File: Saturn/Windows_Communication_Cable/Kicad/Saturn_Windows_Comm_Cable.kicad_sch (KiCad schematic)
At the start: 8 parts, among them J1 SegaSaturn, J2 Windows_RS232

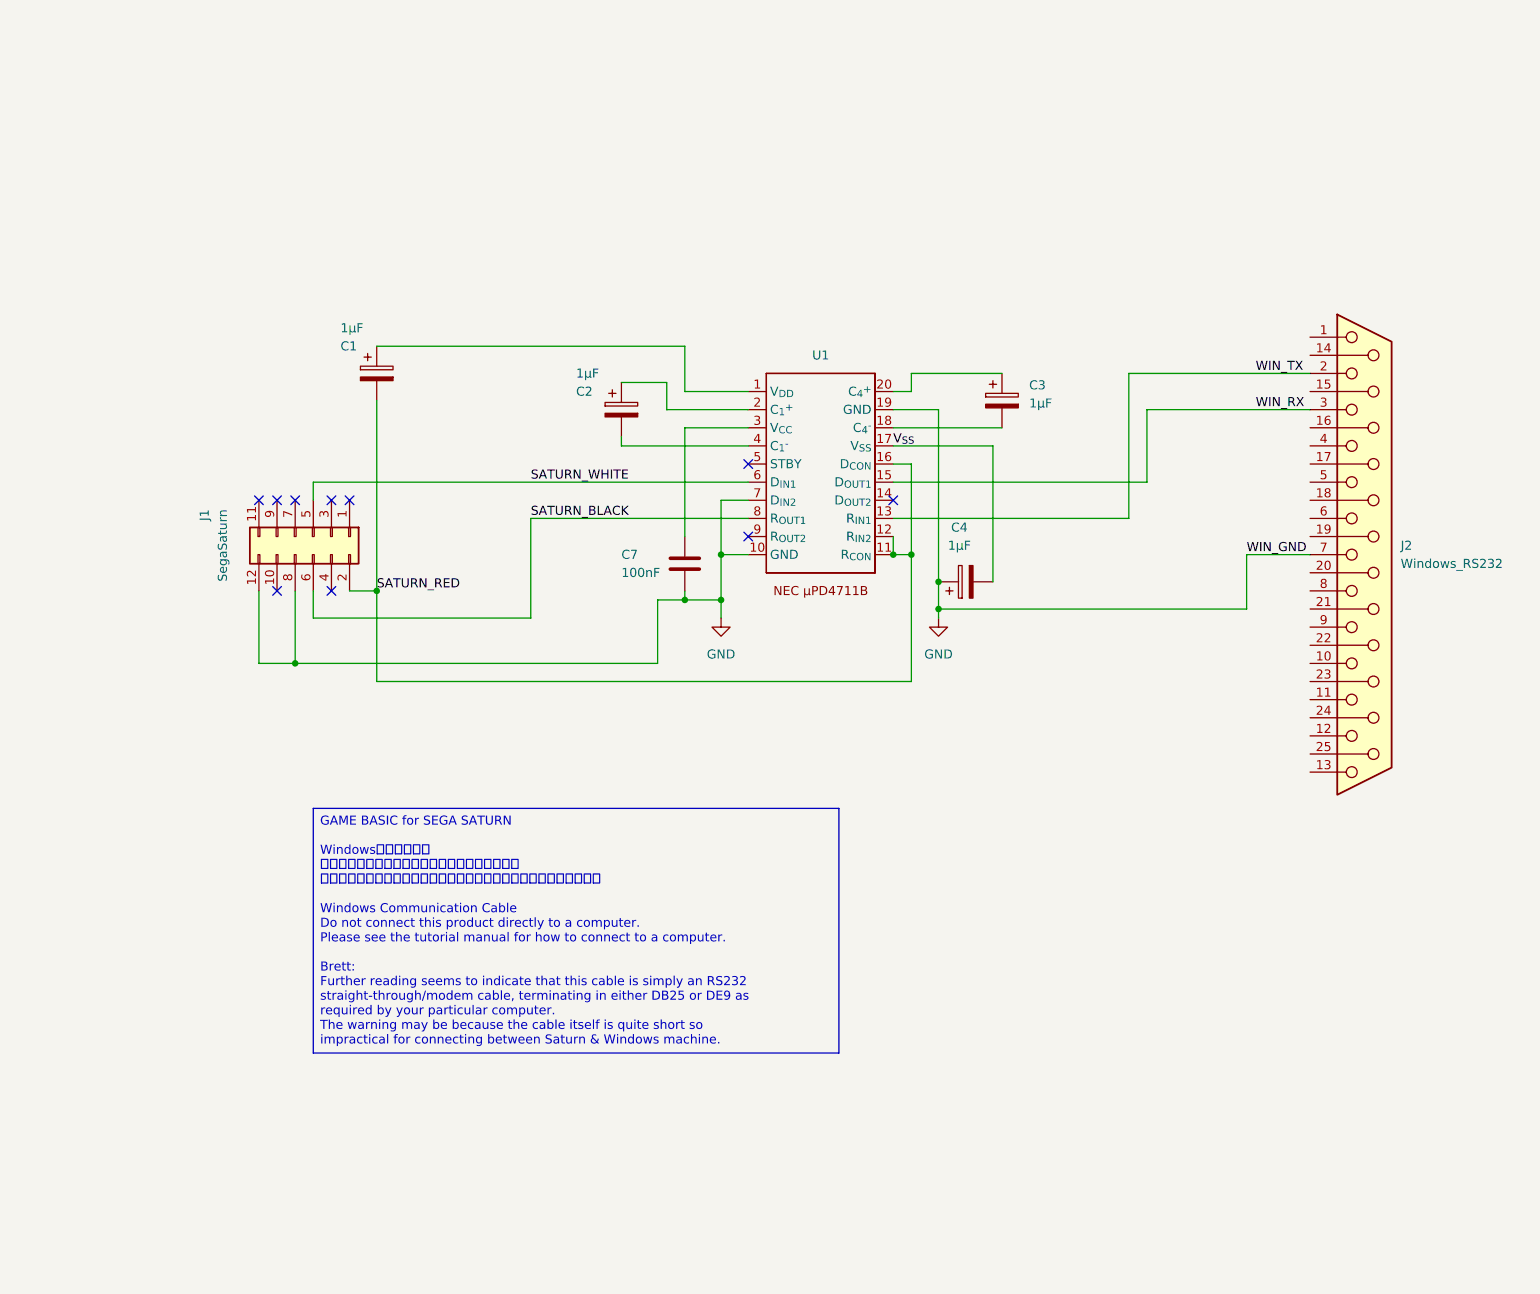
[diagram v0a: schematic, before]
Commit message: Update Saturn_Windows_Comm_Cable.kicad_sch
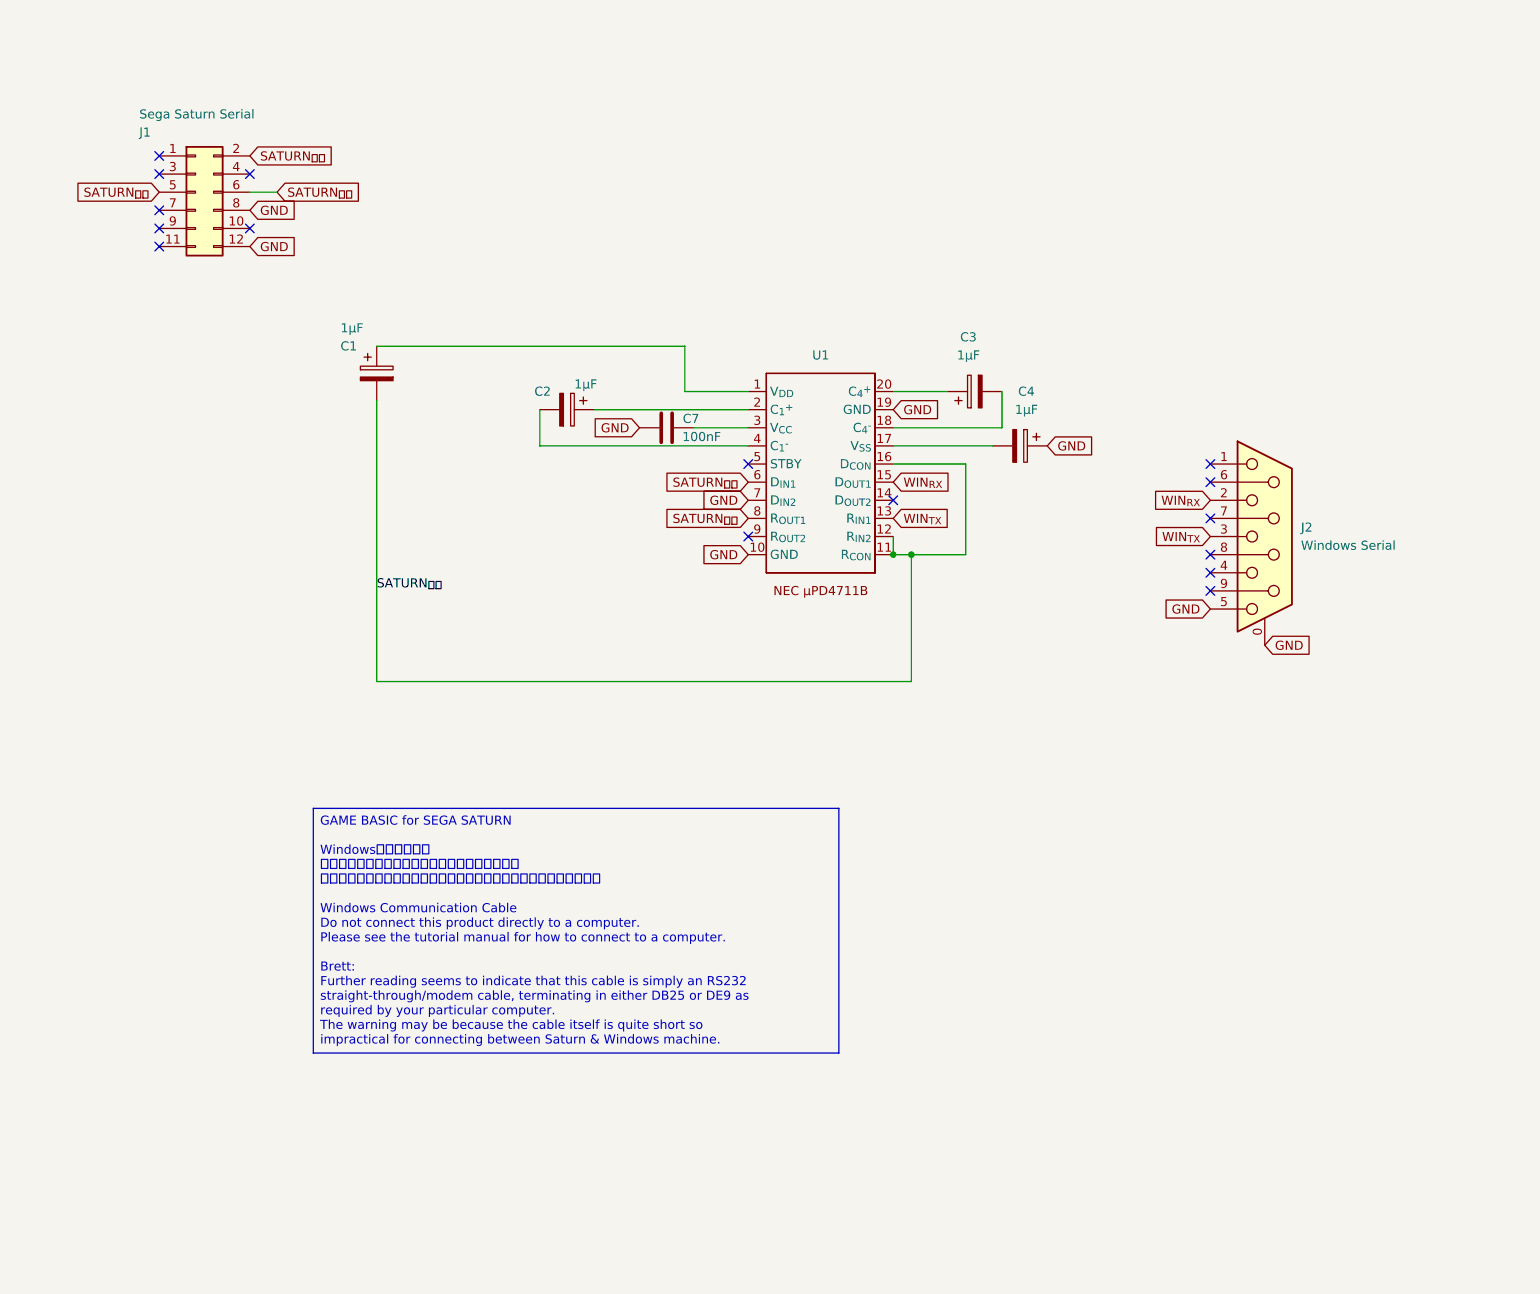
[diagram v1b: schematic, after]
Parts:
- removed J2: Windows_RS232, symbol Connector:DB25_Receptacle
- added J2: Windows Serial, symbol Connector:DE9_Socket_MountingHoles
- J1: value SegaSaturn -> Sega Saturn Serial
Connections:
- net GND: now also C7.2, J2.0 (PAD), J2.5; no longer C7.1
- net at U1.3 (V_{CC}): now also C7.1; no longer C7.2
- net SATURN_BLACK renamed SATURN_{クロ}
- net SATURN_RED renamed SATURN_{アカ}
- net SATURN_WHITE renamed SATURN_{シロ}
- net V_{SS}: no longer names the net of C4.2, U1.17 (V_{SS})
- net WIN_RX renamed WIN_{RX}
- net WIN_{RX}: now also J2.2
- net WIN_TX renamed WIN_{TX}
- net WIN_{TX}: now also J2.3
- no-connect marks 10 -> 16
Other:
- moved on the sheet: C2, C3, C4, C7, J1

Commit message: Revised original SS schematic
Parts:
- removed J1: Sega Saturn Serial, symbol Connector_Generic:Conn_02x06_Odd_Even
- added J1: To Saturn Serial, Connector_PinHeader_2.54mm:PinHeader_1x04_P2.54mm_Vertical, symbol Connector_Generic:Conn_01x04
- added J3: Sega Saturn Serial, symbol Connector_Generic:Conn_02x06_Odd_Even
- C1, C4: footprint (none) -> Capacitor_THT:CP_Radial_D4.0mm_P2.00mm
- C2: renamed from C3; footprint (none) -> Capacitor_THT:CP_Radial_D4.0mm_P2.00mm
- C3: renamed from C2; footprint (none) -> Capacitor_THT:CP_Radial_D4.0mm_P2.00mm
- C5: renamed from C7; footprint (none) -> Capacitor_THT:C_Disc_D5.0mm_W2.5mm_P2.50mm
- J2: footprint (none) -> Connector_Dsub:DSUB-9_Socket_Horizontal_P2.77x2.84mm_EdgePinOffset7.70mm_Housed_MountingHolesOffset9.12mm
- U1: value ~ -> NEC µPD4711B; footprint (none) -> Package_DIP:DIP-20_W7.62mm
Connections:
- net GND: now also J1.3 (Pin_3), J3.12 (Pin_12), J3.8 (Pin_8)
- net SATURN_{アカ}: now also C5.1, U1.3 (V_{CC}), J1.1 (Pin_1), J3.2 (Pin_2); no longer U1.11 (R_{CON}), U1.12 (R_{IN2}), U1.16 (D_{CON})
- net SATURN_{クロ}: now also J1.2 (Pin_2), J3.6 (Pin_6)
- net SATURN_{シロ}: now also J1.4 (Pin_4), J3.5 (Pin_5)
- new net: U1.11 (R_{CON}), U1.12 (R_{IN2}), U1.16 (D_{CON})
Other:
- moved on the sheet: C1, C3, C5, J2
